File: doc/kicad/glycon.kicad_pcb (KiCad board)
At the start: 2 copper layers, 200 x 100 mm, 60 parts, among them J1 Arduino/system bus header, J2 PMOD USBUART conn, J3 Conn_01x02, J4 Conn_02x24_Odd_Even, J5 USB_B, Q1 IRF9540N, Q2 IRF9540N, SW1 SW_Push, SW2 SW_Push, U0 Z80CPU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

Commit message: minor schematic updates
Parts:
- removed R3, R4: 10K, Resistor_THT:R_Axial_DIN0207_L6.3mm_D2.5mm_P10.16mm_Horizontal
- removed U12: CTC-DIP-28, Package_DIP:DIP-28_W15.24mm_Socket
- added C1: 100nF, Capacitor_THT:C_Disc_D4.7mm_W2.5mm_P5.00mm, F.Cu at (200.5, 143.0)
- added C10: 100nF, Capacitor_THT:C_Disc_D4.7mm_W2.5mm_P5.00mm, F.Cu at (150.3, 156.7)
- added C11: 100nF, Capacitor_THT:C_Disc_D4.7mm_W2.5mm_P5.00mm, F.Cu at (150.3, 152.6)
- added C12: 100nF, Capacitor_THT:C_Disc_D4.7mm_W2.5mm_P5.00mm, F.Cu at (168.2, 144.6)
- added C13: 100nF, Capacitor_THT:C_Disc_D4.7mm_W2.5mm_P5.00mm, F.Cu at (114.9, 170.8)
- added C2: 100nF, Capacitor_THT:C_Disc_D4.7mm_W2.5mm_P5.00mm, F.Cu at (114.9, 166.7)
- added C3: 100nF, Capacitor_THT:C_Disc_D4.7mm_W2.5mm_P5.00mm, F.Cu at (160.1, 147.4)
- added C4: 100nF, Capacitor_THT:C_Disc_D4.7mm_W2.5mm_P5.00mm, F.Cu at (200.5, 134.9)
- added C5: 100nF, Capacitor_THT:C_Disc_D4.7mm_W2.5mm_P5.00mm, F.Cu at (160.1, 139.3)
- added C6: 100nF, Capacitor_THT:C_Disc_D4.7mm_W2.5mm_P5.00mm, F.Cu at (160.1, 143.4)
- added C7: 100nF, Capacitor_THT:C_Disc_D4.7mm_W2.5mm_P5.00mm, F.Cu at (160.1, 135.3)
- added C8: 100nF, Capacitor_THT:C_Disc_D4.7mm_W2.5mm_P5.00mm, F.Cu at (200.5, 138.9)
- added C9: 100nF, Capacitor_THT:C_Disc_D4.7mm_W2.5mm_P5.00mm, F.Cu at (138.6, 169.0)
- added H1: MountingHole_Pad, MountingHole:MountingHole_3.2mm_M3_Pad, F.Cu at (27.5, 24.0)
- added H2: MountingHole_Pad, MountingHole:MountingHole_3.2mm_M3_Pad, F.Cu at (219.5, 116.0)
- added H3: MountingHole_Pad, MountingHole:MountingHole_3.2mm_M3_Pad, F.Cu at (27.5, 116.0)
- added H4: MountingHole_Pad, MountingHole:MountingHole_3.2mm_M3_Pad, F.Cu at (123.0, 76.0)
- added H5: MountingHole_Pad, MountingHole:MountingHole_3.2mm_M3_Pad, F.Cu at (219.5, 24.0)
- added IC2: CTC-DIP-28, Package_DIP:DIP-28_W15.24mm_Socket, F.Cu at (90.7, 65.9)
- added J3: Int order hdr, Connector_PinHeader_2.54mm:PinHeader_2x06_P2.54mm_Vertical, F.Cu at (85.5, 152.5)
- added J4: Conn_02x21_Odd_Even, Connector_PinSocket_2.54mm:PinSocket_2x21_P2.54mm_Vertical, F.Cu at (89.7, 127.5)
- added R1: 10K, Resistor_THT:R_Axial_DIN0204_L3.6mm_D1.6mm_P5.08mm_Horizontal, F.Cu at (208.6, 140.2)
- added R10: 10K, Resistor_THT:R_Axial_DIN0204_L3.6mm_D1.6mm_P5.08mm_Horizontal, F.Cu at (200.4, 149.8)
- added R11: 10K, Resistor_THT:R_Axial_DIN0204_L3.6mm_D1.6mm_P5.08mm_Horizontal, F.Cu at (208.6, 137.0)
- added R12: 470, Resistor_THT:R_Axial_DIN0204_L3.6mm_D1.6mm_P5.08mm_Horizontal, F.Cu at (160.0, 151.0)
- added R13: 10K, Resistor_THT:R_Axial_DIN0204_L3.6mm_D1.6mm_P5.08mm_Horizontal, F.Cu at (222.5, 128.5)
- added R5: 10K, Resistor_THT:R_Axial_DIN0204_L3.6mm_D1.6mm_P5.08mm_Horizontal, F.Cu at (200.4, 146.6)
- added R7: 10K, Resistor_THT:R_Axial_DIN0204_L3.6mm_D1.6mm_P5.08mm_Horizontal, F.Cu at (180.3, 133.2)
- added R8: 10K, Resistor_THT:R_Axial_DIN0204_L3.6mm_D1.6mm_P5.08mm_Horizontal, F.Cu at (122.9, 171.1)
- added R9: 10K, Resistor_THT:R_Axial_DIN0204_L3.6mm_D1.6mm_P5.08mm_Horizontal, F.Cu at (150.2, 160.3)
- added RN1: 10K, Resistor_THT:R_Array_SIP10, F.Cu at (104.6, 25.5)
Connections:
- net Net-(U6A-O3)_1 renamed /~{IO_EN1}
- D1 pad 1: Net-(D1-K) -> Net-(D1-Pad1)
- J1 pad 12: /A17 -> unconnected-(J1-Pad12)
- J1 pad 14: /A16 -> unconnected-(J1-Pad14)
- J1 pad 16: /A15 -> unconnected-(J1-Pad16)
- J1 pad 37: /A14 -> unconnected-(J1-Pad37)
- J2 pad 6: unconnected-(J2-Pin_6) -> +5V
- Q1 pad 1: Net-(Q1-G) -> Net-(Q1-Pad1)
- Q2 pad 1: Net-(Q2-G) -> Net-(Q2-Pad1)
- SW1 pad 1: /RESET -> VDD
- SW1 pad 2: VDD -> /RESET
- U0 pad 24: VDD -> unconnected-(U0-Pad24)
- U1 pad 22: Earth -> VDD
- U11 pad 1: /D5 -> /D2
- U11 pad 19: /D7 -> /D0
- U11 pad 2: /D0 -> /D7
- U11 pad 20: /D6 -> /D1
- U11 pad 22: /IEI0 -> /IEO1
- U11 pad 23: Net-(U11-~{INT}) -> Net-(IC2-Pad12)
- U11 pad 3: /D1 -> /D6
- U11 pad 37: Net-(U11-~{M1}) -> /~{M1}
- U11 pad 38: /D2 -> /D5
- U11 pad 39: /D3 -> /D4
- U11 pad 40: /D4 -> /D3
- U5 pad 10: /~{RESET} -> (no net)
- U5 pad 2: Net-(U11-~{INT}) -> Net-(IC2-Pad12)
- U5 pad 4: /~{RESET} -> unconnected-(U5-Pad4)
- U5 pad 5: /~{M1} -> unconnected-(U5-Pad5)
- U5 pad 6: Net-(U11-~{M1}) -> unconnected-(U5-Pad6)
- U5 pad 8: Net-(U8-~{M1}) -> (no net)
- U5 pad 9: /~{M1} -> (no net)
- U7 pad 5: Net-(U11-~{INT}) -> Net-(IC2-Pad12)
- U7 pad 7: /IEI1 -> /IEO2
- U8 pad 16: /~{ASTB} -> unconnected-(U8-Pad16)
- U8 pad 17: /~{BSTB} -> unconnected-(U8-Pad17)
- U8 pad 18: /~{ARDY} -> unconnected-(U8-Pad18)
- U8 pad 21: /~{BRDY} -> unconnected-(U8-Pad21)
- U8 pad 22: /IEI2 -> /IEO3
- U8 pad 23: Net-(U11-~{INT}) -> Net-(IC2-Pad12)
- U8 pad 37: Net-(U8-~{M1}) -> /~{M1}
- X1 pad 8: /CLK -> unconnected-(X1-Pad8)
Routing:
- net /A1: track 272.1 -> 679.0 mm, vias 4 -> 7
- net /IEO2: track 0.00 -> 189.6 mm, vias 0 -> 1
- net /IEI1: track 189.6 -> 0.00 mm, vias 1 -> 0
- net /PGA1: track 160.3 -> 0.00 mm, vias 1 -> 0
- net /PGA0: track 151.9 -> 312.1 mm, vias 0 -> 1
- net /A2: track 153.9 -> 0.00 mm, vias 1 -> 0
- net Net-(U2-Pad31): track 132.9 -> 0.00 mm, vias 2 -> 0
- net /D2: track 277.8 -> 162.2 mm, vias 3 -> 2
- net /D0: track 308.2 -> 206.2 mm, vias 3 -> 1
- net /D5: track 299.7 -> 396.3 mm, vias 2 -> 4
- net /A10: track 89.5 -> 0.00 mm
- net /A9: track 81.0 -> 0.00 mm, vias 1 -> 0
- net /A5: track 74.2 -> 155.3 mm, vias 0 -> 1
- net Net-(U11-~{M1}): track 80.4 -> 0.00 mm, vias 1 -> 0
- net /~{M1}: track 306.8 -> 387.2 mm, vias 6 -> 7
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
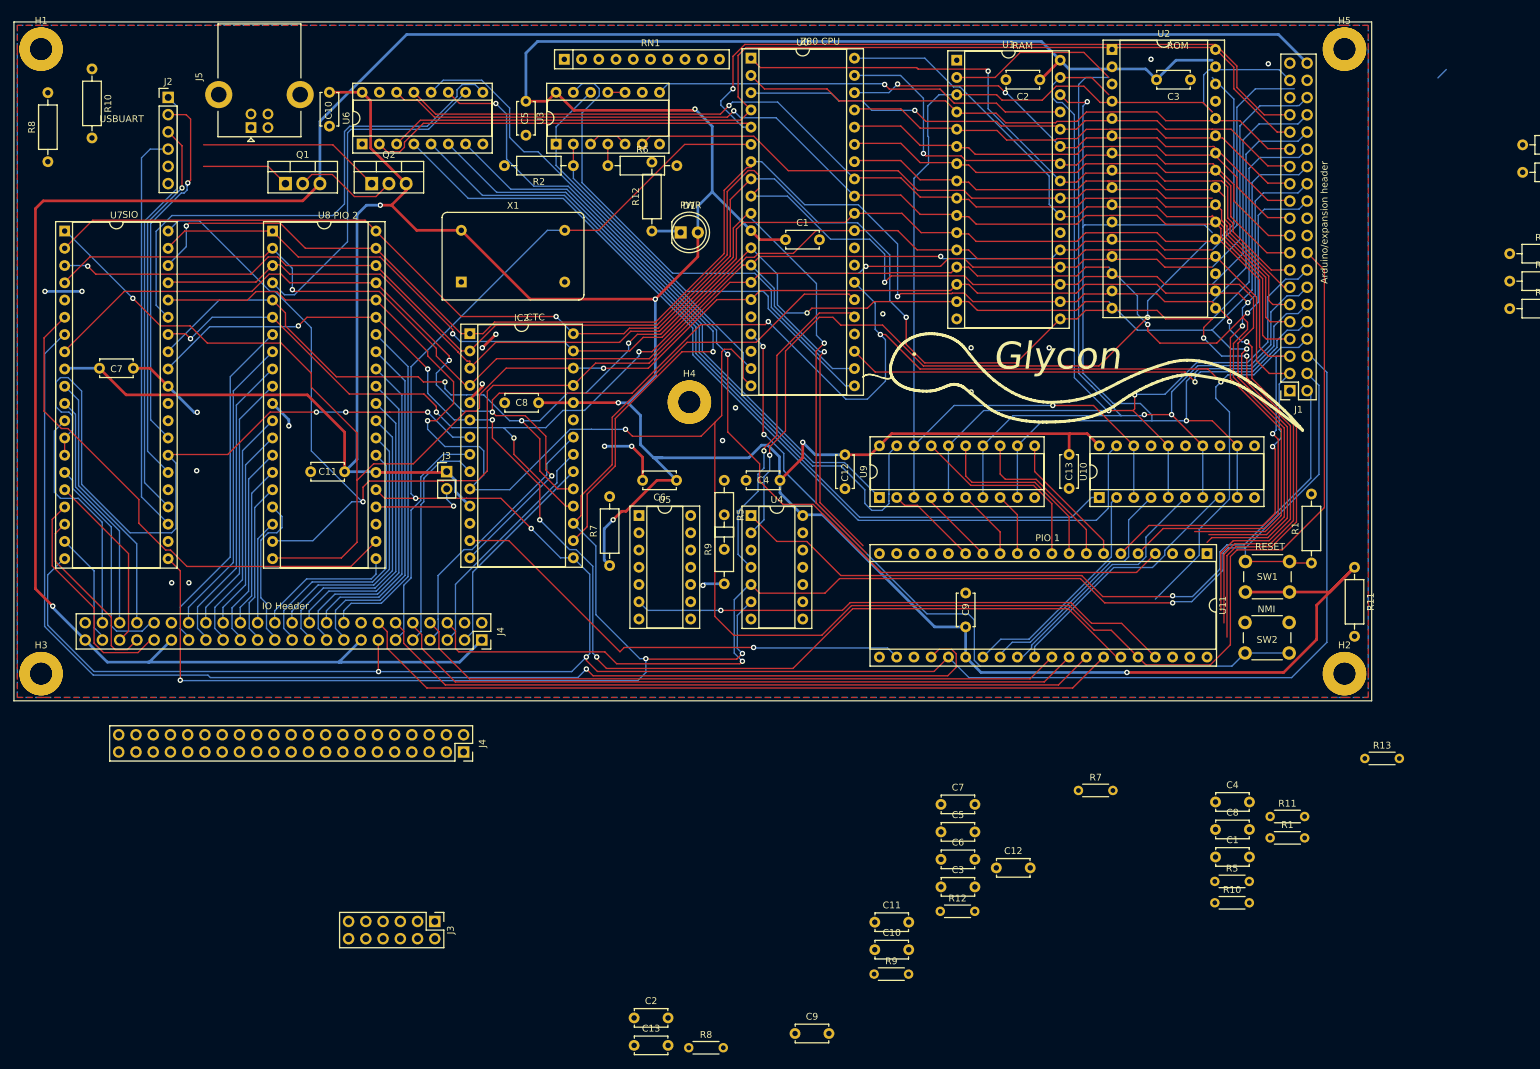
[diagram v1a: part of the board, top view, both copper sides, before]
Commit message: add resistor packs
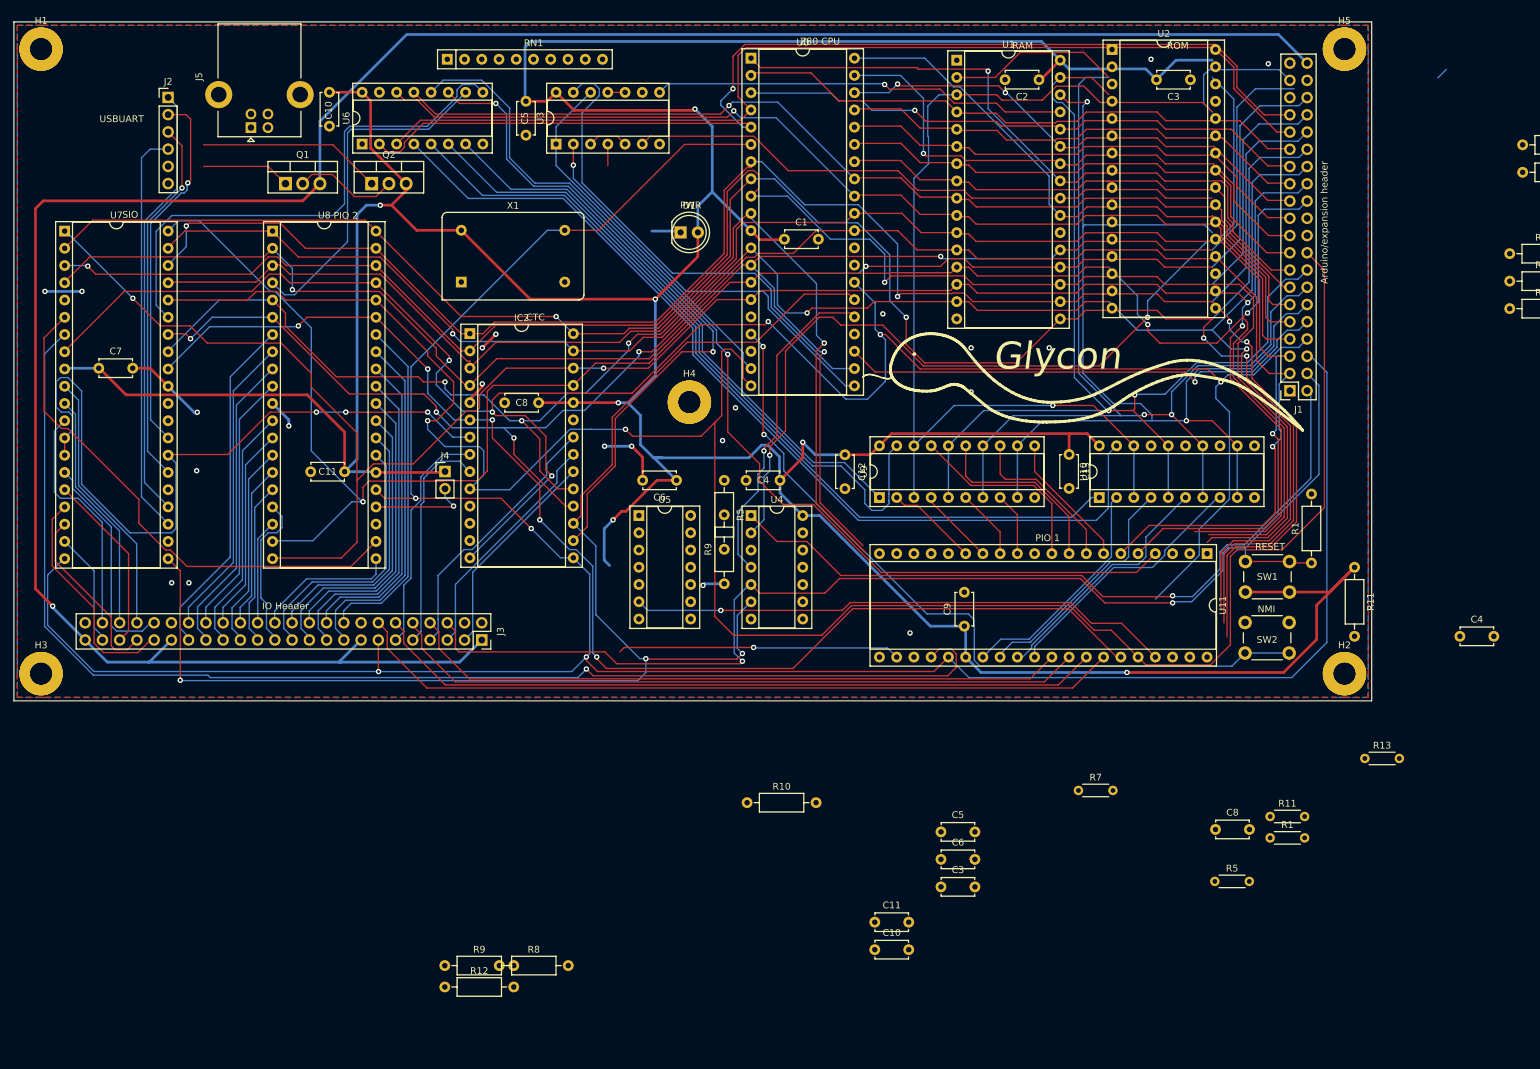
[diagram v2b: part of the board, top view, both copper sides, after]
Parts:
- removed the C1 at (137.2, 52.1)
- removed the C12 at (145.9, 83.8)
- removed the C13 at (178.9, 83.7)
- removed the C2 at (174.6, 28.5)
- removed the C7 at (160.1, 135.3)
- removed the C7 at (36.1, 71.0)
- removed the C9 at (163.7, 109.1)
- removed the J3 at (87.2, 86.2)
- removed the J3 at (85.5, 152.5)
- removed the J4 at (92.4, 111.0)
- removed the J4 at (89.7, 127.5)
- removed the R10 at (35.0, 26.9)
- removed the R12 at (117.5, 50.8)
- removed the R12 at (160.0, 151.0)
- removed R2, R6: 10K, Resistor_THT:R_Axial_DIN0207_L6.3mm_D2.5mm_P10.16mm_Horizontal
- removed the R7 at (111.3, 100.1)
- removed the R8 at (28.5, 40.6)
- removed the R8 at (122.9, 171.1)
- added C7: 100nF, Capacitor_THT:C_Disc_D4.7mm_W2.5mm_P5.00mm, F.Cu at (36.0, 71.0)
- added J3: Conn_02x24_Odd_Even, Connector_PinSocket_2.54mm:PinSocket_2x24_P2.54mm_Vertical, F.Cu at (92.4, 111.0)
- added J4: Conn_01x02, Connector_PinHeader_2.54mm:PinHeader_1x02_P2.54mm_Vertical, F.Cu at (87.0, 86.2)
- added R12: 470, Resistor_THT:R_Axial_DIN0207_L6.3mm_D2.5mm_P10.16mm_Horizontal, F.Cu at (87.0, 162.2)
- added R8: 10K, Resistor_THT:R_Axial_DIN0207_L6.3mm_D2.5mm_P10.16mm_Horizontal, F.Cu at (95.0, 159.0)
- R10, R9: footprint Resistor_THT:R_Axial_DIN0204_L3.6mm_D1.6mm_P5.08mm_Horizontal -> Resistor_THT:R_Axial_DIN0207_L6.3mm_D2.5mm_P10.16mm_Horizontal
- moved C2 150.5 mm to (174.5, 28.5), turned to 180 degrees
- moved C1 111.0 mm to (137.0, 52.0)
- moved C13 108.1 mm to (178.9, 83.7), turned to -90 degrees
- moved R10 70.5 mm to (131.5, 135.0)
- moved C9 65.0 mm to (163.5, 109.0), turned to 90 degrees
- moved C12 64.8 mm to (145.9, 83.8), turned to -90 degrees
- moved R9 63.3 mm to (87.0, 159.0)
- moved C4 43.5 mm to (236.5, 110.5)
- moved RN1 17.2 mm to (87.3, 25.5)
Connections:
- net /~{IO_EN1} renamed Net-(U6-Pad9)
- IC2 pad 11: /IEO0 -> VDD
- IC2 pad 13: /IEI0 -> /IEO1
- RN1 pad 3: Earth -> Net-(U0-Pad22)
- RN1 pad 6: unconnected-(RN1-Pad6) -> /A3
- RN1 pad 7: unconnected-(RN1-Pad7) -> /A2
- RN1 pad 8: unconnected-(RN1-Pad8) -> /PGA1
- RN1 pad 9: unconnected-(RN1-Pad9) -> /PGA0
- U0 pad 24: unconnected-(U0-Pad24) -> VDD
- U11 pad 37: /~{M1} -> /~{PIO_M1}
- U5 pad 4: unconnected-(U5-Pad4) -> /~{M1}
- U5 pad 5: unconnected-(U5-Pad5) -> /~{RESET}
- U5 pad 6: unconnected-(U5-Pad6) -> /~{PIO_M1}
- U7 pad 6: /IEI2 -> /IEO3
- U7 pad 7: /IEO2 -> /IEI1
- U8 pad 16: unconnected-(U8-Pad16) -> /~{ASTB}
- U8 pad 17: unconnected-(U8-Pad17) -> /~{BSTB}
- U8 pad 18: unconnected-(U8-Pad18) -> /ARDY
- U8 pad 21: unconnected-(U8-Pad21) -> /BRDY
- U8 pad 37: /~{M1} -> /~{PIO_M1}
- X1 pad 7: Earth -> unconnected-(X1-Pad7)
- X1 pad 8: unconnected-(X1-Pad8) -> /CLK
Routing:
- net /PGA1: track 0.00 -> 312.1 mm, vias 0 -> 1
- net /PGA0: track 312.1 -> 0.00 mm, vias 1 -> 0
- net /IEO2: track 189.6 -> 0.00 mm, vias 1 -> 0
- net /IEI1: track 0.00 -> 189.6 mm, vias 0 -> 1
- net /~{PIO_M1}: track 0.00 -> 80.4 mm, vias 0 -> 1
- net /~{M1}: track 387.2 -> 306.8 mm, vias 7 -> 6
- net /IEO3: track 0.00 -> 77.0 mm
- net /IEI2: track 77.0 -> 0.00 mm
- net /IEO1: track 70.5 -> 41.6 mm
- net unconnected-(U8-Pad16): track 23.6 -> 0.00 mm
- net /~{ASTB}: track 0.00 -> 23.6 mm
- net unconnected-(U8-Pad17): track 22.6 -> 0.00 mm
- net /~{BSTB}: track 0.00 -> 22.6 mm
- net /~{BRDY}: track 20.7 -> 0.00 mm
- net /BRDY: track 0.00 -> 20.7 mm
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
